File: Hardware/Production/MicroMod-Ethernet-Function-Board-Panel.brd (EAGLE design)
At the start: 135.1 x 154.6 mm, 618 parts, among them J1 MAGJACK_SYM, J10 MICROMOD_STANDARD, J11 MICROMOD_STANDARD, J12 MAGJACK_SYM, J2 MICROMOD_STANDARD, J3 MAGJACK_SYM, J4 MICROMOD_STANDARD, J5 MAGJACK_SYM, J6 MICROMOD_STANDARD, J7 MAGJACK_SYM, J8 MICROMOD_STANDARD, J9 MAGJACK_SYM, Q1 220mA/50V/3.5Ω, Q10 220mA/50V/3.5Ω, Q11 20V/4.2A/52mΩ/1.4W, Q12 220mA/50V/3.5Ω, Q2 20V/4.2A/52mΩ/1.4W, Q3 220mA/50V/3.5Ω, Q4 20V/4.2A/52mΩ/1.4W, Q5 20V/4.2A/52mΩ/1.4W, Q6 220mA/50V/3.5Ω, Q7 20V/4.2A/52mΩ/1.4W, Q8 220mA/50V/3.5Ω, Q9 20V/4.2A/52mΩ/1.4W, U1 EEPROM, U10 W5500, U11 3.3V, U12 POE_PSU-DP990X, U13 EEPROM, U14 W5500, U15 3.3V, U16 POE_PSU-DP990X, U17 EEPROM, U18 W5500, U19 3.3V, U2 EEPROM, U20 POE_PSU-DP990X, U21 EEPROM, U22 W5500, U23 3.3V, U24 POE_PSU-DP990X, U3 W5500, U4 3.3V, U5 POE_PSU-DP990X, U6 W5500, U7 3.3V, U8 POE_PSU-DP990X, U9 EEPROM, Y1 25MHz, Y2 25MHz, Y3 25MHz, Y4 25MHz, Y5 25MHz, Y6 25MHz

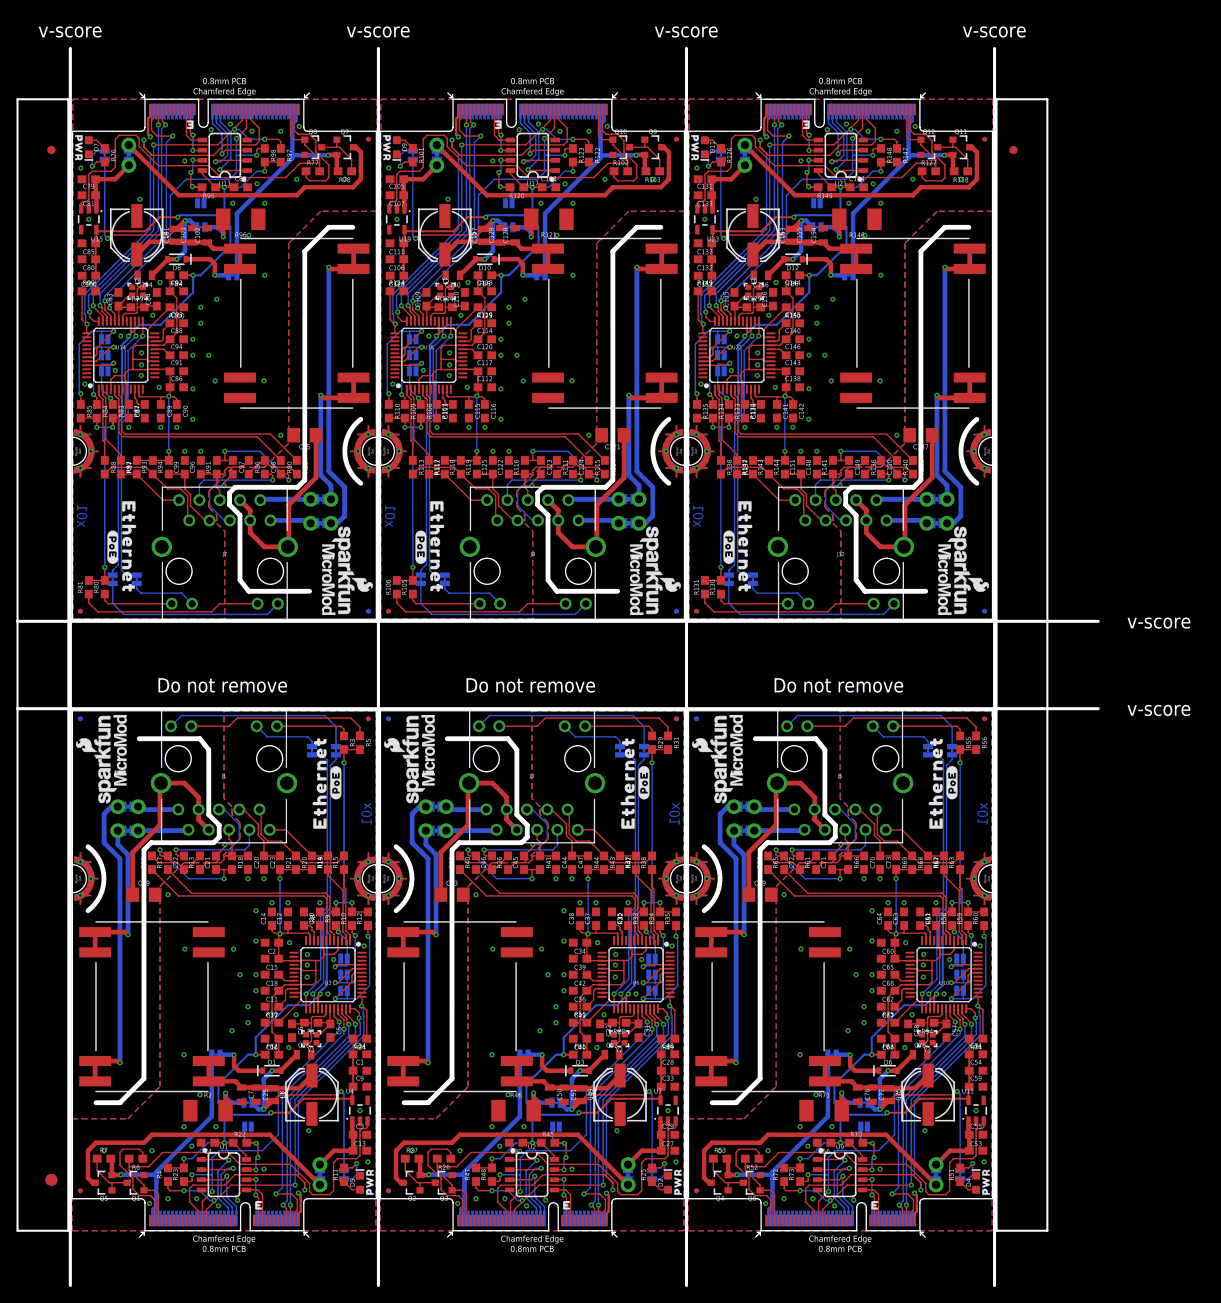
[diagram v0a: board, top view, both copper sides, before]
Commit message: Add ESD to TX/RX, landmarks to PoE module, additional GND thermals.
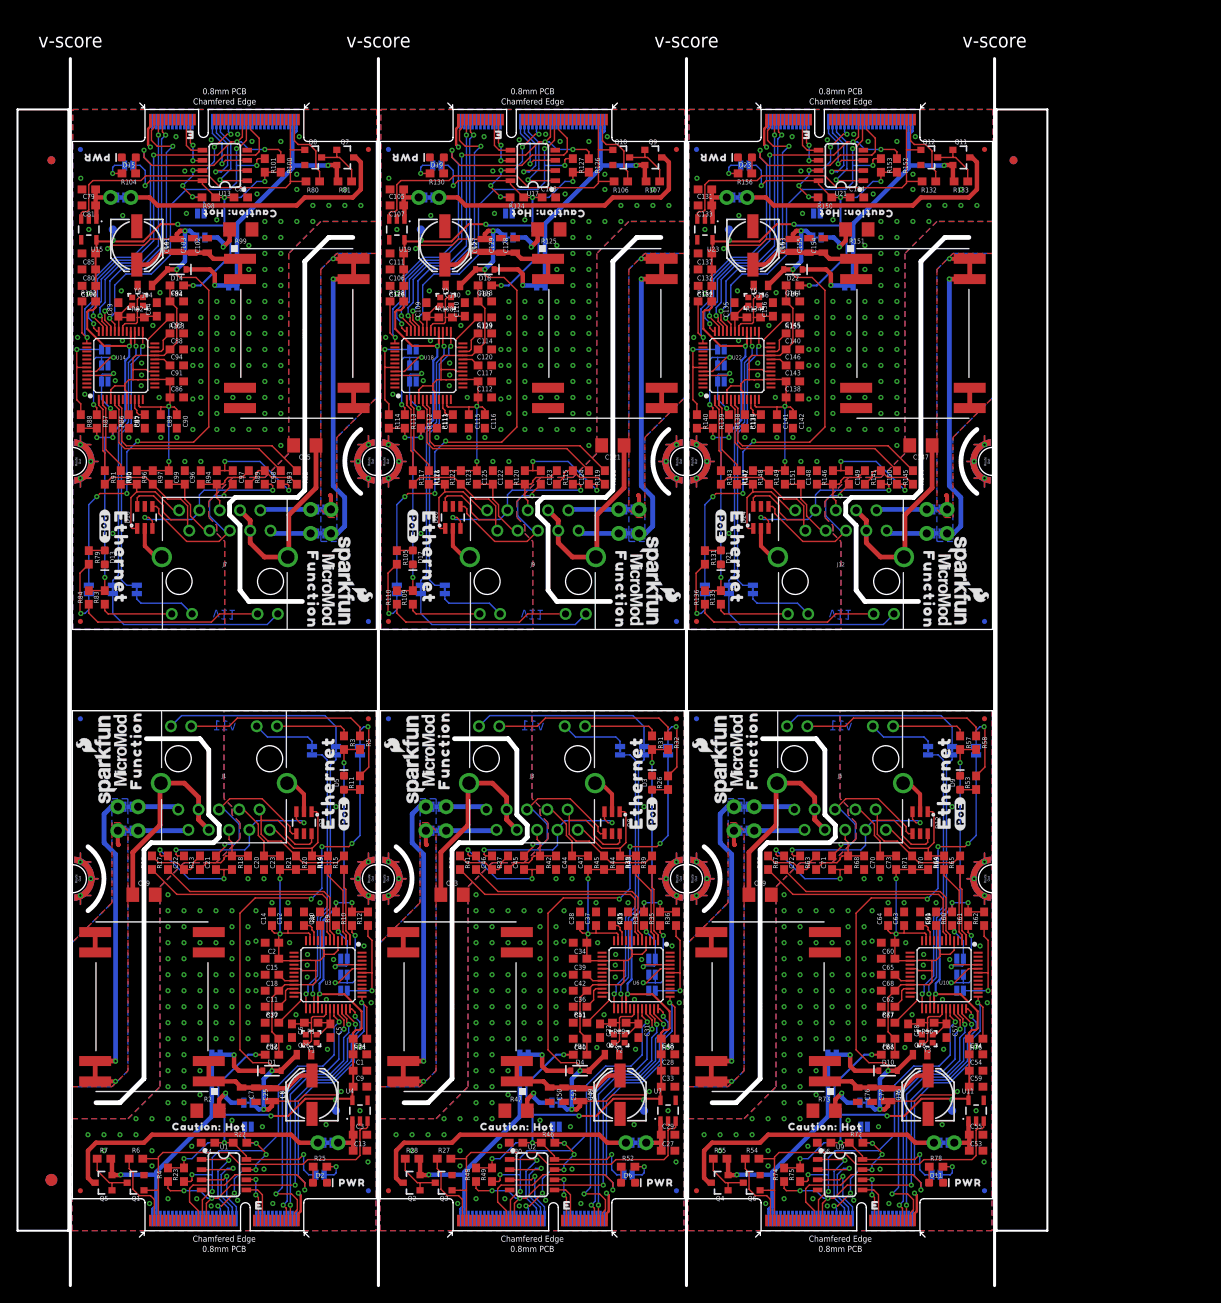
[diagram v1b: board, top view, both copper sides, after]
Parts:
- removed JP25, JP30: JUMPER-SMT_2_NO_SILK, SparkFun-Jumpers:SMT-JUMPER_2_NO_SILK
- removed JP26, JP27, JP28: (no value), SparkFun-Jumpers:SMT-JUMPER_2_NO_SILK
- removed JP29: PoE System, SparkFun-Jumpers:SMT-JUMPER_2_NC_TRACE_SILK
- added D13, D17, D21: Yellow, SparkFun-LED:LED-0603
- added D14, D18, D22: 3A/10V/280mV, SparkFun-DiscreteSemi:SOD-323
- added D15, D19, D23: RED, SparkFun-LED:LED-0603
- added D16, D20, D24: DT1042-04SO, SparkFun-DiscreteSemi:SOT-23-6
- added POE, POE1, POE2, POE3, POE4, POE5: (no value), SparkFun-Jumpers:SMT-JUMPER_2_NC_TRACE_SILK
- added PWR_LED, PWR_LED1, PWR_LED2, PWR_LED3, PWR_LED4, PWR_LED5: JUMPER-SMT_2_NC_TRACE_SILK, SparkFun-Jumpers:SMT-JUMPER_2_NC_TRACE_SILK
- added R151: 49.9 1/2W, SparkFun-Resistors:1206
- added R152, R153, R154, R155: 10k, SparkFun-Resistors:0603
- added R156: 1k, SparkFun-Resistors:0603
- added TP1, TP2, TP3, TP4, TP5, TP6: TEST-POINT3X4, SparkFun-Connectors:PAD.03X.04
- added U$115, U$142: (no value), output:12
- added U$116, U$143: (no value), output:23
- added U$117, U$119, U$144, U$146: (no value), output:ETHERNET0
- added U$118, U$120, U$145, U$147: (no value), output:#POE#0
- added U$121, U$148: (no value), output:#POWER_CARRIER#0
- added U$122, U$149: (no value), output:#DUMMY_LOAD#0
- added U$123, U$150: (no value), output:#WP#0
- added U$124, U$151: (no value), output:#ACT#0
- added U$125, U$152: (no value), output:#LNK#1
- added U$126, U$153: (no value), output:CAUTION#0
- added U$127, U$154: (no value), output:HOT#1
- added U$128, U$155: (no value), output:#PWR#0
- added U$129, U$156: (no value), output:#_POE#0
- added U$130, U$157: (no value), output:POE0
- added U$131, U$158: (no value), output:PWR1
- added U$132, U$159: (no value), output:#0
- added U$133, U$160: (no value), output:#1
- added U$134, U$135, U$161, U$162: (no value), output:FUNCTION0
- added U$136, U$137: (no value), SparkFun-MicroMod:MICROMOD_LOGO_.35
- added U$138: (no value), output:#MEAS#3
- added U$139: (no value), output:PWR0
- added U$140: (no value), output:#PMODE#0
- added U$141: (no value), output:01
- D12, D8: value 3A/10V/280mV -> DT1042-04SO; device SparkFun-DiscreteSemi:SOD-323 -> SparkFun-DiscreteSemi:SOT-23-6
- D3: value 3A/10V/280mV -> Yellow; device SparkFun-DiscreteSemi:SOD-323 -> SparkFun-LED:LED-0603
- D4: value RED -> 3A/10V/280mV; device SparkFun-LED:LED-0603 -> SparkFun-DiscreteSemi:SOD-323
- D5, D9: value RED -> Yellow
- D6: value 3A/10V/280mV -> RED; device SparkFun-DiscreteSemi:SOD-323 -> SparkFun-LED:LED-0603
- D7: value RED -> DT1042-04SO; device SparkFun-LED:LED-0603 -> SparkFun-DiscreteSemi:SOT-23-6
- ISO1, ISO10, ISO11, ISO12, ISO2, ISO3, ISO4, ISO5, ISO6, ISO7, ISO8, ISO9, MEAS, MEAS1, MEAS2, MEAS3, MEAS4, MEAS5: value (none) -> JUMPER-COMBO_2_NC_TRACE
- J1, J12, J3, J5, J7, J9: value MAGJACK_SYM -> MAGJACK-POE; device Ethernet:MAGJACK-STR_LED -> SparkFun-Connectors:MAGJACK-SYM_LED
- JP1, JP11, JP12, JP13, JP16, JP17, JP18, JP2, JP21, JP22, JP23, JP3, JP6, JP7, JP8: value (none) -> JUMPER-SMT_2_NO_SILK
- JP14, JP19, JP24, JP4, JP9: value PoE System -> JUMPER-SMT_2_NO_SILK; device SparkFun-Jumpers:SMT-JUMPER_2_NC_TRACE_SILK -> SparkFun-Jumpers:SMT-JUMPER_2_NO_SILK
- LOAD, LOAD1, LOAD2, LOAD3, LOAD4, LOAD5, POE_LED, POE_LED1, POE_LED2, POE_LED3, POE_LED4, POE_LED5: value (none) -> JUMPER-SMT_2_NC_TRACE_SILK
- R101, R106, R126, R51, R55, R76, R80, R81: value 1k -> 10k
- R104, R79: value 1M -> 1k
- R107, R132: value 12.4k -> 10k
- R108, R134: value 10k -> 1M
- R109, R110, R135, R26, R52, R53, R58, R78, R83, R84: value 10k -> 1k
- R111: value 49.9 -> 12.4k
- R112, R113, R114, R138, R139, R140, R62, R87, R88: value 33 -> 10k
- R115, R37, R63, R89: value 33 -> 49.9
- R116, R117, R118, R142, R143, R41, R66, R67, R91, R92, R93: value 49.9 -> 33
- R119, R144: value 10 -> 33
- R120, R122, R147, R148, R70, R95: value 10k -> 49.9
- R121, R146, R96: value 510 -> 49.9; device SparkFun-Resistors:2010 -> SparkFun-Resistors:0603
- R123, R149, R45, R97: value 10k -> 10
- R125, R47, R73, R99: value 10k -> 49.9 1/2W; device SparkFun-Resistors:0603 -> SparkFun-Resistors:1206
- R129, R28, R54: value 1M -> 10k
- R136: value 49.9 -> 1k
- R137: value 33 -> 12.4k
- R145: value 10k -> 33
- R2: value 510 -> 49.9 1/2W; device SparkFun-Resistors:2010 -> SparkFun-Resistors:1206
- R29, R56: value 1k -> 1M
- R32, R57: value 12.4k -> 1k
- R33, R59, R85: value 10k -> 12.4k
- R36, R61, R86: value 49.9 -> 10k
- R44, R69, R94: value 10 -> 49.9
- R46: value 510 -> 10k; device SparkFun-Resistors:2010 -> SparkFun-Resistors:0603
- R71: value 510 -> 10; device SparkFun-Resistors:2010 -> SparkFun-Resistors:0603
- R82: value 12.4k -> 1M
- U$100, U$21: device output:#PWR#0 -> output:HOT#1
- U$101, U$22: device output:#PMODE#0 -> output:#PWR#0
- U$102, U$23: device output:01 -> output:#_POE#0
- U$103: device output:12 -> output:POE0
- U$104: device output:23 -> output:PWR1
- U$105: device output:ETHERNET0 -> output:#0
- U$106: device output:#POE#0 -> output:#1
- U$107, U$26: device output:ETHERNET0 -> output:FUNCTION0
- U$108, U$27: device output:#POE#0 -> output:FUNCTION0
- U$109: device output:#POWER_CARRIER#0 -> SparkFun-MicroMod:MICROMOD_LOGO_.35
- U$110: device output:#DUMMY_LOAD#0 -> SparkFun-MicroMod:MICROMOD_LOGO_.35
- U$111: device output:#WP#0 -> output:#MEAS#3
- U$112: device output:#ACT#0 -> output:PWR0
- U$113: device output:#LNK#1 -> output:#PMODE#0
- U$114, U$87: device output:#POE#0 -> output:01
- U$19, U$50: device output:#POE#0 -> output:#0
- U$20, U$99: device output:PWR0 -> output:CAUTION#0
- U$24: device output:12 -> output:PWR1
- U$25: device output:23 -> output:#1
- U$29: device output:ETHERNET0 -> output:PWR0
- U$30: device output:#POE#0 -> output:#PMODE#0
- U$31: device output:#POWER_CARRIER#0 -> output:01
- U$32: device output:#DUMMY_LOAD#0 -> output:12
- U$33: device output:#WP#0 -> output:23
- U$34: device output:#ACT#0 -> output:ETHERNET0
- U$35: device output:#LNK#1 -> output:#POE#0
- U$36: device output:#POE#0 -> output:ETHERNET0
- U$38: device SparkFun-MicroMod:MICROMOD_LOGO_.35 -> output:#POE#0
- U$39: device SparkFun-MicroMod:MICROMOD_LOGO_.35 -> output:#POWER_CARRIER#0
- U$40: device output:#MEAS#3 -> output:#DUMMY_LOAD#0
- U$41: device output:PWR0 -> output:#WP#0
- U$42: device output:#PWR#0 -> output:#ACT#0
- U$43: device output:#PMODE#0 -> output:#LNK#1
- U$44: device output:01 -> output:CAUTION#0
- U$45: device output:12 -> output:HOT#1
- U$46: device output:23 -> output:#PWR#0
- U$47: device output:ETHERNET0 -> output:#_POE#0
- U$48, U$76: device output:#POE#0 -> output:POE0
- U$49: device output:ETHERNET0 -> output:PWR1
- U$51: device output:#POWER_CARRIER#0 -> output:#1
- U$52: device output:#DUMMY_LOAD#0 -> output:FUNCTION0
- U$53: device output:#WP#0 -> output:FUNCTION0
- U$54: device output:#ACT#0 -> SparkFun-MicroMod:MICROMOD_LOGO_.35
- U$55: device output:#LNK#1 -> SparkFun-MicroMod:MICROMOD_LOGO_.35
- U$56: device output:#POE#0 -> output:#MEAS#3
- U$57: device SparkFun-MicroMod:MICROMOD_LOGO_.35 -> output:PWR0
- U$58: device SparkFun-MicroMod:MICROMOD_LOGO_.35 -> output:#PMODE#0
- U$59: device output:#MEAS#3 -> output:01
- U$60: device output:PWR0 -> output:12
- U$61: device output:#PWR#0 -> output:23
- U$62: device output:#PMODE#0 -> output:ETHERNET0
- U$64: device output:01 -> output:#POE#0
- U$65: device output:12 -> output:ETHERNET0
- U$66: device output:23 -> output:#POE#0
- U$67: device output:ETHERNET0 -> output:#POWER_CARRIER#0
- U$68, U$95: device output:#POE#0 -> output:#DUMMY_LOAD#0
- U$69: device output:ETHERNET0 -> output:#WP#0
- U$70: device output:#POE#0 -> output:#ACT#0
- U$71: device output:#POWER_CARRIER#0 -> output:#LNK#1
- U$72: device output:#DUMMY_LOAD#0 -> output:CAUTION#0
- U$73: device output:#WP#0 -> output:HOT#1
- U$74: device output:#ACT#0 -> output:#PWR#0
- U$75: device output:#LNK#1 -> output:#_POE#0
- U$77: device SparkFun-MicroMod:MICROMOD_LOGO_.35 -> output:PWR1
- U$78: device SparkFun-MicroMod:MICROMOD_LOGO_.35 -> output:#0
- U$79: device output:#MEAS#3 -> output:#1
- U$80: device output:PWR0 -> output:FUNCTION0
- U$81: device output:#PWR#0 -> output:FUNCTION0
- U$82: device output:#PMODE#0 -> SparkFun-MicroMod:MICROMOD_LOGO_.35
- U$83: device output:01 -> SparkFun-MicroMod:MICROMOD_LOGO_.35
- U$84: device output:12 -> output:#MEAS#3
- U$85: device output:23 -> output:PWR0
- U$86: device output:ETHERNET0 -> output:#PMODE#0
- U$88: device output:ETHERNET0 -> output:12
- U$89: device output:#POE#0 -> output:23
- U$9: device output:#PWR#0 -> output:POE0
- U$90: device output:#POWER_CARRIER#0 -> output:ETHERNET0
- U$91: device output:#DUMMY_LOAD#0 -> output:#POE#0
- U$92: device output:#WP#0 -> output:ETHERNET0
- U$93: device output:#ACT#0 -> output:#POE#0
- U$94: device output:#LNK#1 -> output:#POWER_CARRIER#0
- U$96: device SparkFun-MicroMod:MICROMOD_LOGO_.35 -> output:#WP#0
- U$97: device SparkFun-MicroMod:MICROMOD_LOGO_.35 -> output:#ACT#0
- U$98: device output:#MEAS#3 -> output:#LNK#1
- U12, U16, U20, U24, U5, U8: device Ethernet:DP990X -> SparkFun-IC-Power:DP990X
- moved R76 155.1 mm to (113.0, 24.0), turned to 180 degrees
- moved U$60 149.5 mm to (108.9, 32.0), flipped to the bottom, turned to 0 degrees
- moved U$61 145.6 mm to (108.9, 30.0), turned to 0 degrees
- moved R78 144.7 mm to (108.0, 8.00), turned to 0 degrees
- moved U$73 139.7 mm to (97.5, 13.1), flipped to the top, turned to 0 degrees
- moved U$59 138.0 mm to (108.9, 34.0), turned to 0 degrees
- moved JP15 135.8 mm to (4.05, 110.2)
- moved U$72 132.7 mm to (92.6, 13.0), flipped to the top, turned to 0 degrees
- moved D11 132.6 mm to (108.0, 6.00), turned to 0 degrees
- moved JP13 131.3 mm to (4.05, 106.2), turned to 0 degrees
- moved R77 128.4 mm to (102.0, 26.0)
- moved U$74 126.4 mm to (104.8, 7.00), turned to 0 degrees
- moved JP14 125.3 mm to (4.05, 108.2)
- moved U$69 124.5 mm to (96.4, 13.0), turned to 0 degrees
- moved U$64 118.5 mm to (111.0, 52.1), flipped to the top, turned to 90 degrees
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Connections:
- net N$103 renamed PW1+5
- net N$104 renamed PW1-5
- net N$14 renamed PW1+
- net N$18 renamed PW1-
- net N$31 renamed PW1+1
- net N$32 renamed PW1-1
- net N$49 renamed PW1+2
- net N$50 renamed PW1-2
- net N$67 renamed PW1+3
- net N$68 renamed PW1-3
- net N$85 renamed PW1+4
- net N$86 renamed PW1-4
- removed net N$105: JP30.2, R145.2, U21.7
- removed net N$108: R150.2, U22.23
- removed net N$26 (its old number): R32.2, U6.10
- removed net N$30 (its old number): LOAD1.1, R46.2
- removed net N$43 (its old number): J5.11, R55.1
- removed net N$44 (its old number): R57.2, U10.10
- removed net N$47 (its old number): D6.C, JP14.1
- removed net N$48 (its old number): LOAD2.1, R71.2
- removed net N$60 (its old number): J7.13, R81.1
- removed net N$61 (its old number): J7.11, R80.1
- removed net N$65 (its old number): D8.C, JP19.1
- removed net N$77 (its old number): C110.1, R104.2, U18.30, Y5.3
- removed net N$78 (its old number): J9.13, R106.1
- removed net N$94 (its old number): C135.1, R129.1, U22.31, Y6.1
- removed net N$95 (its old number): C136.1, R129.2, U22.30, Y6.3
- removed net N$98 (its old number): R132.2, U22.10
- new net EWP: J11.40, JP5.2, R22.2, U1.7
- new net EWP1: J2.40, JP8.2, R46.2, U2.7
- new net EWP2: J4.40, JP12.2, R72.2, U9.7
- new net EWP3: J6.40, JP16.2, R98.2, U13.7
- new net EWP4: J8.40, JP20.2, R124.2, U17.7
- new net EWP5: J10.40, JP24.2, R150.2, U21.7
- new net N$100: R155.2, U22.23
- new net N$14: D3.A, R26.1
- new net N$18: Q2.1, Q3.3, R28.1
- new net N$28: D4.C, POE1.1
- new net N$32: R51.2, U6.23
- new net N$34: D6.A, R52.1
- new net N$35: POE_LED2.1, R53.2
- new net N$45: D10.C, POE2.1
- new net N$46: LOAD2.1, R73.2
- new net N$49: R77.2, U10.23
- new net N$50: PWR_LED2.1, R78.2
- new net N$52: POE_LED3.1, R79.2
- new net N$53: D13.A, R79.1
- new net N$63: LOAD3.1, R99.2
- new net N$67: PWR_LED3.1, R104.2
- new net N$68: D15.A, R104.1
- new net N$70: D17.A, R105.1
- new net N$71: Q10.3, Q9.1, R107.1
- new net N$85: D19.A, R130.1
- new net N$86: POE_LED5.1, R131.2
- new net N$88: Q11.1, Q12.3, R133.1
- new net N$89: C135.1, R134.1, U22.31, Y6.1
- net 3.3V: now also PWR_LED.2, TP1.1
- net 3.3V1: now also PWR_LED1.2, R32.2, R36.2, R46.1, R50.2, TP2.1; no longer R29.2, R33.2, R45.1, R47.2
- net 3.3V2: now also PWR_LED2.2, R57.2, R61.2, R62.2, R72.1, R75.2, R76.2, TP3.1; no longer R55.2, R56.2, R59.2, R70.1, R72.2, R73.2
- net 3.3V3: now also PWR_LED3.2, R100.2, R101.2, R102.2, R86.2, R87.2, R88.2, R98.1, TP4.1; no longer R80.2, R81.2, R85.2, R95.1, R97.2, R98.2, R99.2
- net 3.3V4: now also PWR_LED4.2, R112.2, R113.2, R114.2, R124.1, R126.2, R127.2, R128.2, TP5.1; no longer R105.2, R106.2, R108.2, R120.1, R122.2, R123.2, R124.2
- net 3.3V5: now also PWR_LED5.2, R136.2, R138.2, R139.2, R140.2, R150.1, R152.2, R153.2, R154.2, TP6.1; no longer R130.2, R131.2, R133.2, R134.2, R145.1, R147.2, R148.2, R149.2
- net 3.3V_IN1: now also R27.1; no longer R26.1
- net 3.3V_IN2: now also R54.1; no longer R52.1
- net 3.3V_IN3: now also R80.1; no longer R77.1
- net 3.3V_IN4: now also R106.1; no longer R102.1
- net 3.3V_IN5: now also R132.1; no longer R127.1
- net 5V_FILTER1: now also D4.A; no longer D3.A
- net 5V_FILTER2: now also D10.A; no longer D6.A
- net 5V_FILTER3: now also D14.A; no longer D8.A
- net 5V_FILTER4: now also D18.A; no longer D10.A
- net 5V_FILTER5: now also D22.A; no longer D12.A
- net ETH_!CS!1: now also R49.1; no longer R48.1
- net ETH_!CS!2: now also R75.1; no longer R73.1
- net ETH_!CS!3: now also R101.1; no longer R98.1
- net ETH_!CS!4: now also R127.1; no longer R123.1
- net ETH_!CS!5: now also R153.1; no longer R148.1
- net ETH_!INT!1: now also R48.1; no longer R47.1
- net ETH_!INT!2: now also R74.1; no longer R72.1
- net ETH_!INT!3: now also R100.1; no longer R97.1
- net ETH_!INT!4: now also R126.1; no longer R122.1
- net ETH_!INT!5: now also R152.1; no longer R147.1
- net ETH_!RST!1: now also R50.1; no longer R49.1
- net ETH_!RST!2: now also R76.1; no longer R74.1
- net ETH_!RST!3: now also R102.1; no longer R99.1
- net ETH_!RST!4: now also R128.1; no longer R124.1
- net ETH_!RST!5: now also R154.1; no longer R149.1
- net GND: now also D2.C
- net GND-ISO: now also D7.2
- net GND-ISO1: now also D8.2
- net GND-ISO2: now also D12.2
- net GND-ISO3: now also D16.2
- net GND-ISO4: now also D20.2
- net GND-ISO5: now also D24.2
- net GND1: now also D3.C, D6.C, JP4.1, R33.1, R47.1, R51.1; no longer D2.C, JP10.1, R32.1, R46.1, R50.1
- net GND2: now also D11.C, D9.C, JP10.1, JP9.1, R59.1, R73.1, R77.1; no longer D4.C, JP13.1, JP15.1, R57.1, R71.1, R75.1
- net GND3: now also D13.C, D15.C, JP13.1, JP14.1, JP15.1, R103.1, R85.1, R99.1; no longer D7.C, JP17.1, JP18.1, JP20.1, R100.1, R82.1, R96.1
- net GND4: now also D17.C, D19.C, JP17.1, JP18.1, JP19.1, JP20.1, R111.1, R129.1; no longer D9.C, JP21.1, JP22.1, JP23.1, JP25.1, R107.1, R121.1
- net GND5: now also D21.C, D23.C, JP21.1, JP22.1, JP23.1, JP24.1, R137.1, R151.1, R155.1; no longer D11.C, JP26.1, JP27.1, JP28.1, JP30.1, R132.1, R146.1, R150.1
- net N$101: now also PWR_LED5.1, R156.2; no longer D12.C, JP29.1
- net N$102: now also D23.A, R156.1; no longer LOAD5.1, R146.2
- net N$12: now also POE_LED1.1, R26.2; no longer JP5.2, R22.2, U1.7
- net N$19: now also PWR_LED.1; no longer POE_LED1.1
- net N$21: now also C31.1, R29.1, U6.31, Y2.1; no longer Q2.1, Q3.3, R27.1
- net N$22: now also C32.1, R29.2, U6.30, Y2.3; no longer C31.1, R28.1, U6.31, Y2.1
- net N$23: now also J3.13, R32.1; no longer C32.1, R28.2, U6.30, Y2.3
- net N$24: now also J3.11; no longer J3.13
- net N$25: now also R33.2, U6.10; no longer J3.11, R29.1
- net N$29: now also LOAD1.1, R47.2; no longer D3.C, JP9.1
- net N$33: now also PWR_LED1.1, R52.2; no longer JP10.2, R45.2, U2.7
- net N$36: now also D9.A, R53.1; no longer R50.2, U6.23
- net N$37: now also Q4.1, Q6.3, R55.1; no longer POE_LED2.1, R51.2
- net N$38: now also C57.1, R56.1, U10.31, Y3.1; no longer D4.A, R51.1
- net N$39: now also C58.1, R56.2, U10.30, Y3.3; no longer Q4.1, Q6.3, R53.1
- net N$40: now also J5.13, R58.1; no longer C57.1, R54.1, U10.31, Y3.1
- net N$41: now also J5.11, R57.1; no longer C58.1, R54.2, U10.30, Y3.3
- net N$42: now also R59.2, U10.10; no longer J5.13, R56.1
- net N$51: now also D11.A, R78.1; no longer JP15.2, R70.2, U9.7
- net N$54: now also Q7.1, Q8.3, R81.1; no longer R75.2, U10.23
- net N$55: now also C83.1, R82.1, U14.31, Y4.1; no longer POE_LED3.1, R76.2
- net N$56: now also C84.1, R82.2, U14.30, Y4.3; no longer D7.A, R76.1
- net N$57: now also J7.13, R84.1; no longer Q7.1, Q8.3, R78.1
- net N$58: now also J7.11, R83.1; no longer C83.1, R79.1, U14.31, Y4.1
- net N$59: now also R85.2, U14.10; no longer C84.1, R79.2, U14.30, Y4.3
- net N$62: now also D14.C, POE3.1; no longer R82.2, U14.10
- net N$66: now also R103.2, U14.23; no longer LOAD3.1, R96.2
- net N$69: now also POE_LED4.1, R105.2; no longer JP20.2, R95.2, U13.7
- net N$7: now also POE.1; no longer JP4.1
- net N$72: now also C109.1, R108.1, U18.31, Y5.1; no longer R100.2, U14.23
- net N$73: now also C110.1, R108.2, U18.30, Y5.3; no longer POE_LED4.1, R101.2
- net N$74: now also J9.13, R110.1; no longer D9.A, R101.1
- net N$75: now also J9.11, R109.1; no longer Q10.3, Q9.1, R103.1
- net N$76: now also R111.2, U18.10; no longer C109.1, R104.1, U18.31, Y5.1
- net N$79: now also D18.C, POE4.1; no longer J9.11, R105.1
- net N$80: now also LOAD4.1, R125.2; no longer R107.2, U18.10
- net N$83: now also R129.2, U18.23; no longer D10.C, JP24.1
- net N$84: now also PWR_LED4.1, R130.2; no longer LOAD4.1, R121.2
- net N$87: now also D21.A, R131.1; no longer JP25.2, R120.2, U17.7
- net N$90: now also C136.1, R134.2, U22.30, Y6.3; no longer R125.2, U18.23
- net N$91: now also J12.13, R136.1; no longer POE_LED5.1, R126.2
- net N$92: now also J12.11, R135.1; no longer D11.A, R126.1
- net N$93: now also R137.2, U22.10; no longer Q11.1, Q12.3, R128.1
- net N$96: now also D22.C, POE5.1; no longer J12.13, R131.1
- net N$97: now also LOAD5.1, R151.2; no longer J12.11, R130.1
- net PMODE10: now also JP14.2, R87.1; no longer JP17.2, R84.1
- net PMODE11: now also JP15.2, R88.1; no longer JP18.2, R85.1
- net PMODE12: now also JP17.2, R112.1; no longer JP21.2, R108.1
- net PMODE13: now also JP18.2, R113.1; no longer JP22.2, R109.1
- net PMODE14: now also JP19.2, R114.1; no longer JP23.2, R110.1
- net PMODE15: now also JP21.2, R138.1; no longer JP26.2, R133.1
- net PMODE16: now also JP22.2, R139.1; no longer JP27.2, R134.1
- net PMODE17: now also JP23.2, R140.1; no longer JP28.2, R135.1
- net PMODE3: now also JP4.2, R34.1; no longer JP6.2, R33.1
- net PMODE4: now also JP6.2, R35.1; no longer JP7.2, R34.1
- net PMODE5: now also JP7.2, R36.1; no longer JP8.2, R35.1
- net PMODE6: now also JP9.2, R60.1; no longer JP11.2, R58.1
- net PMODE7: now also JP10.2, R61.1; no longer JP12.2, R59.1
- net PMODE8: now also JP11.2, R62.1; no longer JP13.2, R60.1
- net PMODE9: now also JP13.2, R86.1; no longer JP16.2, R83.1
- net PWR_EN1: now also R27.2; no longer R26.2
- net PWR_EN2: now also R54.2; no longer R52.2
- net PWR_EN3: now also R80.2; no longer R77.2
- net PWR_EN4: now also R106.2; no longer R102.2
- net PWR_EN5: now also R132.2; no longer R127.2
- net RCT1: now also R37.1, R42.1; no longer R36.1, R41.1
- net RCT2: now also R63.1, R68.1; no longer R61.1, R66.1
- net RCT3: now also R89.1, R94.1; no longer R86.1, R91.1
- net RCT4: now also R115.1, R120.1; no longer R111.1, R116.1
- net RCT5: now also R146.1; no longer R136.1
- net RD+: now also D7.3
- net RD+1: now also D8.3
- net RD+2: now also D12.3
- net RD+3: now also D16.3
- net RD+4: now also D20.3
- net RD+5: now also D24.3
- net RD-: now also D7.4
- net RD-1: now also D8.4
- net RD-2: now also D12.4
- net RD-3: now also D16.4
- net RD-4: now also D20.4
- net RD-5: now also D24.4
- net RXN10: now also R145.1; no longer R140.1
- net RXN11: now also R145.2, R146.2; no longer R140.2, R141.2
- net RXN2: now also R41.1; no longer R40.1
- net RXN3: now also R42.2; no longer R40.2
- net RXN4: now also R67.1; no longer R65.1
- net RXN5: now also R67.2, R68.2; no longer R65.2, R66.2
- net RXN6: now also R93.1; no longer R90.1
- net RXN7: now also R93.2, R94.2; no longer R90.2, R91.2
- net RXN8: now also R119.1; no longer R115.1
- net RXN9: now also R119.2, R120.2; no longer R115.2, R116.2
- net RXP10: now also R144.1; no longer R139.1
- net RXP11: now also R141.2, R144.2; no longer R136.2, R139.2
- net RXP2: now also R40.1; no longer R39.1
- net RXP3: now also R37.2, R40.2; no longer R36.2, R39.2
- net RXP4: now also R66.1; no longer R64.1
- net RXP5: now also R63.2, R66.2; no longer R61.2, R64.2
- net RXP6: now also R92.1; no longer R89.1
- net RXP7: now also R92.2; no longer R86.2
- net RXP8: now also R118.1; no longer R114.1
- net RXP9: now also R115.2, R118.2; no longer R111.2, R114.2
- net TCT1: now also R45.1; no longer R44.1
- net TCT2: now also R71.1; no longer R69.1
- net TCT3: now also R97.1; no longer R94.1
- net TCT4: now also R123.1; no longer R119.1
- net TCT5: now also R149.1; no longer R144.1
- net TD+: now also D7.1
- net TD+1: now also D8.1, R38.2, R43.1; no longer R37.2, R42.1
- net TD+2: now also D12.1, R64.2, R69.1; no longer R62.2, R67.1
- net TD+3: now also D16.1, R90.2, R95.1; no longer R87.2, R92.1
- net TD+4: now also D20.1, R116.2, R121.1; no longer R112.2, R117.1
- net TD+5: now also D24.1, R142.2, R147.1; no longer R137.2, R142.1
- net TD-: now also D7.6
- net TD-1: now also D8.6, R39.2, R44.1; no longer R38.2, R43.1
- net TD-2: now also D12.6, R65.2, R70.1; no longer R63.2, R68.1
- net TD-3: now also D16.6, R91.2, R96.1; no longer R88.2, R93.1
- net TD-4: now also D20.6, R117.2, R122.1; no longer R113.2, R118.1
- net TD-5: now also D24.6, R143.2, R148.1; no longer R138.2, R143.1
- net TXN1: now also R39.1; no longer R38.1
- net TXN2: now also R65.1; no longer R63.1
- net TXN3: now also R91.1; no longer R88.1
- net TXN4: now also R117.1; no longer R113.1
- net TXN5: now also R143.1; no longer R138.1
- net TXP1: now also R38.1; no longer R37.1
- net TXP2: now also R64.1; no longer R62.1
- net TXP3: now also R90.1; no longer R87.1
- net TXP4: now also R116.1; no longer R112.1
- net TXP5: now also R142.1; no longer R137.1
- net VCCA1: now also R45.2; no longer R42.2
- net VCCA2: now also R70.2, R71.2; no longer R67.2, R68.2
- net VCCA3: now also R95.2, R96.2, R97.2; no longer R92.2, R93.2, R94.2
- net VCCA4: now also R121.2, R122.2, R123.2; no longer R117.2, R118.2, R119.2
- net VCCA5: now also R147.2, R148.2, R149.2; no longer R142.2, R143.2, R144.2
- net VCC_IN: now also POE.2; no longer JP4.2
- net VCC_IN1: now also POE1.2, R28.2; no longer JP9.2, R27.2
- net VCC_IN2: now also POE2.2, R55.2; no longer JP14.2, R53.2
- net VCC_IN3: now also POE3.2, R81.2; no longer JP19.2, R78.2
- net VCC_IN4: now also POE4.2, R107.2; no longer JP24.2, R103.2
- net VCC_IN5: now also POE5.2, R133.2; no longer JP29.2, R128.2
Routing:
- net 5V_FILTER1: track 33.1 -> 76.8 mm, vias 3 -> 6
- net 5V_FILTER2: track 33.1 -> 76.8 mm, vias 3 -> 6
- net 5V_FILTER: track 33.1 -> 76.8 mm, vias 3 -> 6
- net 5V_FILTER5: track 33.1 -> 76.8 mm, vias 3 -> 6
- net 5V_FILTER4: track 33.1 -> 76.8 mm, vias 3 -> 6
- net 5V_FILTER3: track 33.1 -> 76.8 mm, vias 3 -> 6
- net N$78 (its old number): track 23.1 -> 0.00 mm
- net N$60 (its old number): track 23.1 -> 0.00 mm
- net N$74: track 2.43 -> 23.1 mm
- net N$42: track 23.1 -> 2.86 mm
- net EWP5: track 0.00 -> 19.3 mm, vias 0 -> 5
- net EWP3: track 0.00 -> 19.3 mm, vias 0 -> 5
- net EWP4: track 0.00 -> 19.3 mm, vias 0 -> 5
- net EWP2: track 0.00 -> 19.3 mm, vias 0 -> 5
- net EWP1: track 0.00 -> 19.3 mm, vias 0 -> 5
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- added copper zone on layer 1, net PW1+
- added copper zone on layer 1, net PW1+1
- added copper zone on layer 1, net PW1+2
- added copper zone on layer 1, net PW1+3
- added copper zone on layer 1, net PW1+4
- added copper zone on layer 1, net PW1+5
- added copper zone on layer 16, net PW1-
- added copper zone on layer 16, net PW1-1
- added copper zone on layer 16, net PW1-2
- added copper zone on layer 16, net PW1-3
- added copper zone on layer 16, net PW1-4
- added copper zone on layer 16, net PW1-5
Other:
- board size 135.1 x 154.6 mm -> 128.7 x 153.4 mm
- board text added: "v11"
- board text removed: "Do not remove"
- board text removed: "x01"
